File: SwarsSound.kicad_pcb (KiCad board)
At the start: 2 copper layers, 292.1 x 227.3 mm, 168 parts, among them P1 Main_Connector, P2 aud_con, P3 edge_con, Q1 2N3906f, Q2 2N3906f, Q3 2N3904, Q4 2N3904

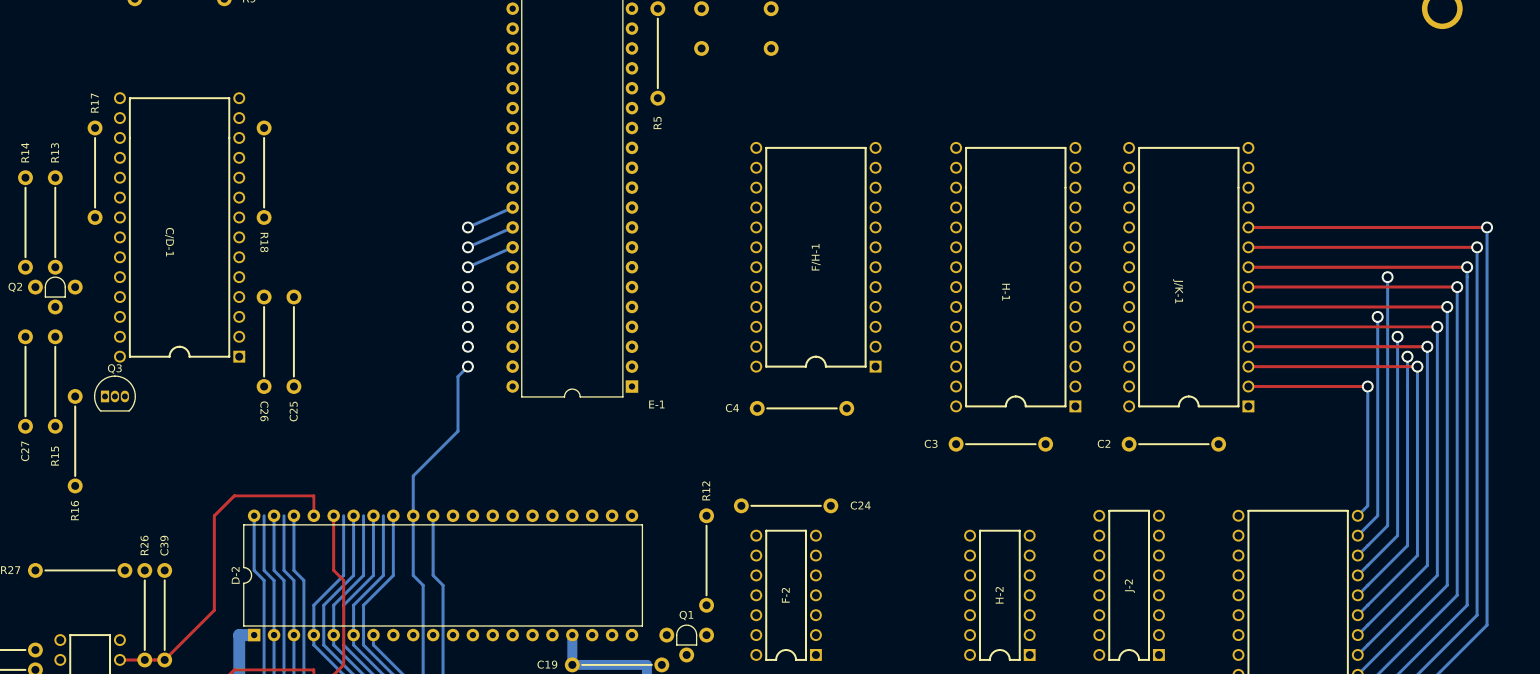
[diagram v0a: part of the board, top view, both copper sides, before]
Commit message: ROM and RAM buses
Not complete
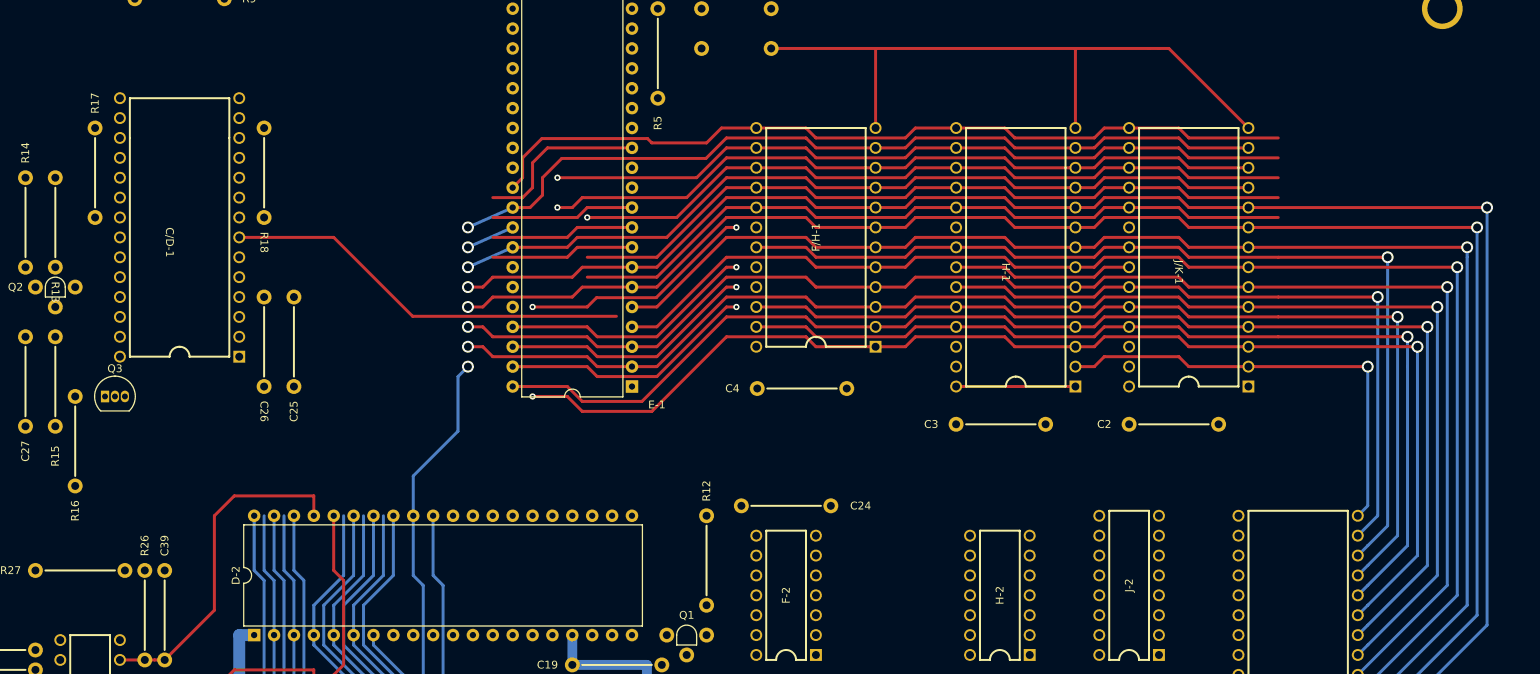
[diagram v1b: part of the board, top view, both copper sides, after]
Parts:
- moved C4 2.54 mm to (211.6, 87.9)
- moved F/H-1 2.54 mm to (212.7, 68.6)
- moved C2 2.54 mm to (259.1, 92.5)
- moved C3 2.54 mm to (237.0, 92.5)
- moved H-1 2.54 mm to (237.6, 71.1)
- moved J/K-1 2.54 mm to (259.7, 71.1)
- moved R13 1.27 mm to (115.6, 66.0), turned to 180 degrees
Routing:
- net SA4: track 77.1 -> 186.7 mm, vias 1 -> 2
- net SA5: track 152.1 -> 261.7 mm, vias 1 -> 2
- net SA1: track 179.6 -> 289.2 mm, vias 1 -> 2
- net SA0: track 180.2 -> 289.8 mm, vias 1 -> 2
- net GND: track 80.0 -> 188.7 mm
- net SD3: track 91.3 -> 196.8 mm
- net SA6: track 63.4 -> 167.8 mm
- net SD2: track 81.8 -> 183.4 mm
- net SA7: track 56.5 -> 157.8 mm, vias 1 -> 2
- net SD0: track 81.8 -> 182.1 mm
- net SD4: track 91.3 -> 187.6 mm, vias 0 -> 1
- net SD7: track 98.7 -> 193.3 mm
- net SD6: track 98.7 -> 193.3 mm
- net SD5: track 98.7 -> 192.2 mm, vias 0 -> 1
- net SD1: track 81.8 -> 175.3 mm, vias 1 -> 2
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
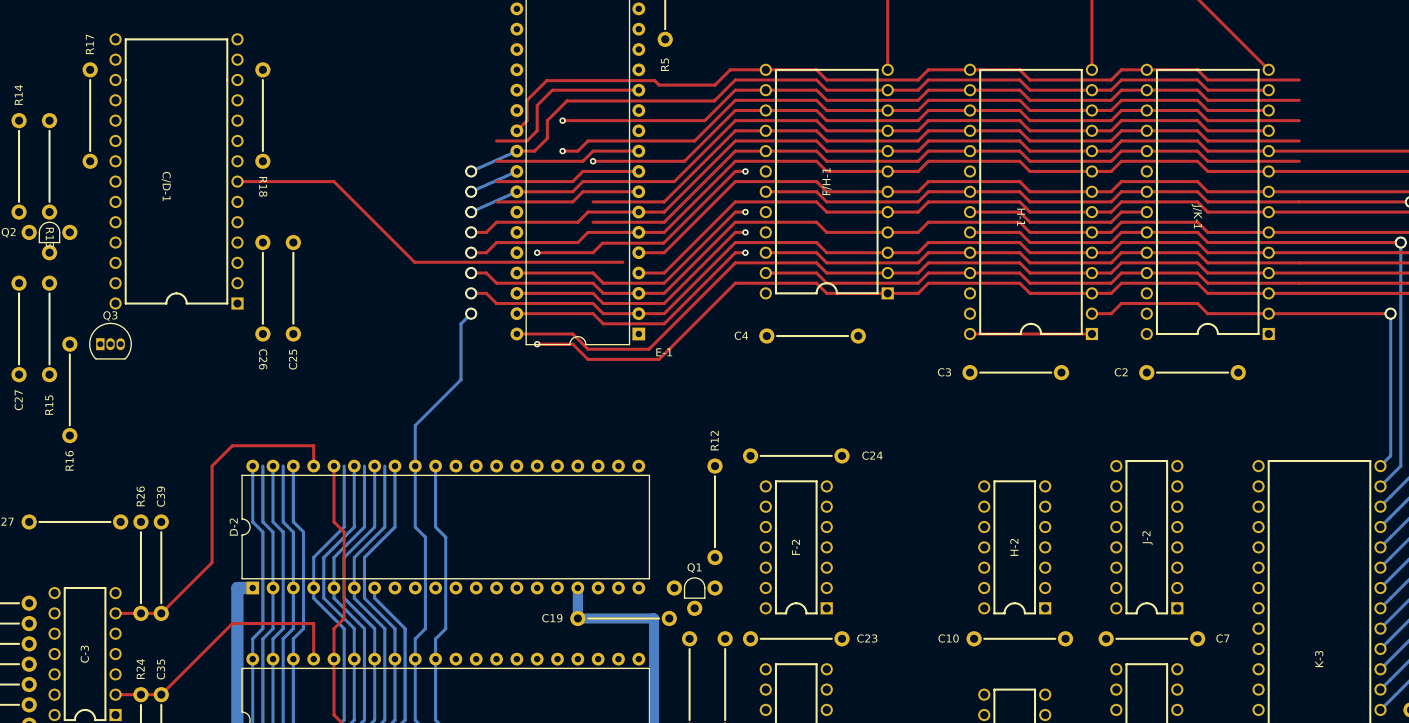
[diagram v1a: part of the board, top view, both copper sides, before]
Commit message: fixes
fixed RAM (pin '28' -> 24) and finished RAM/ROM data bus.
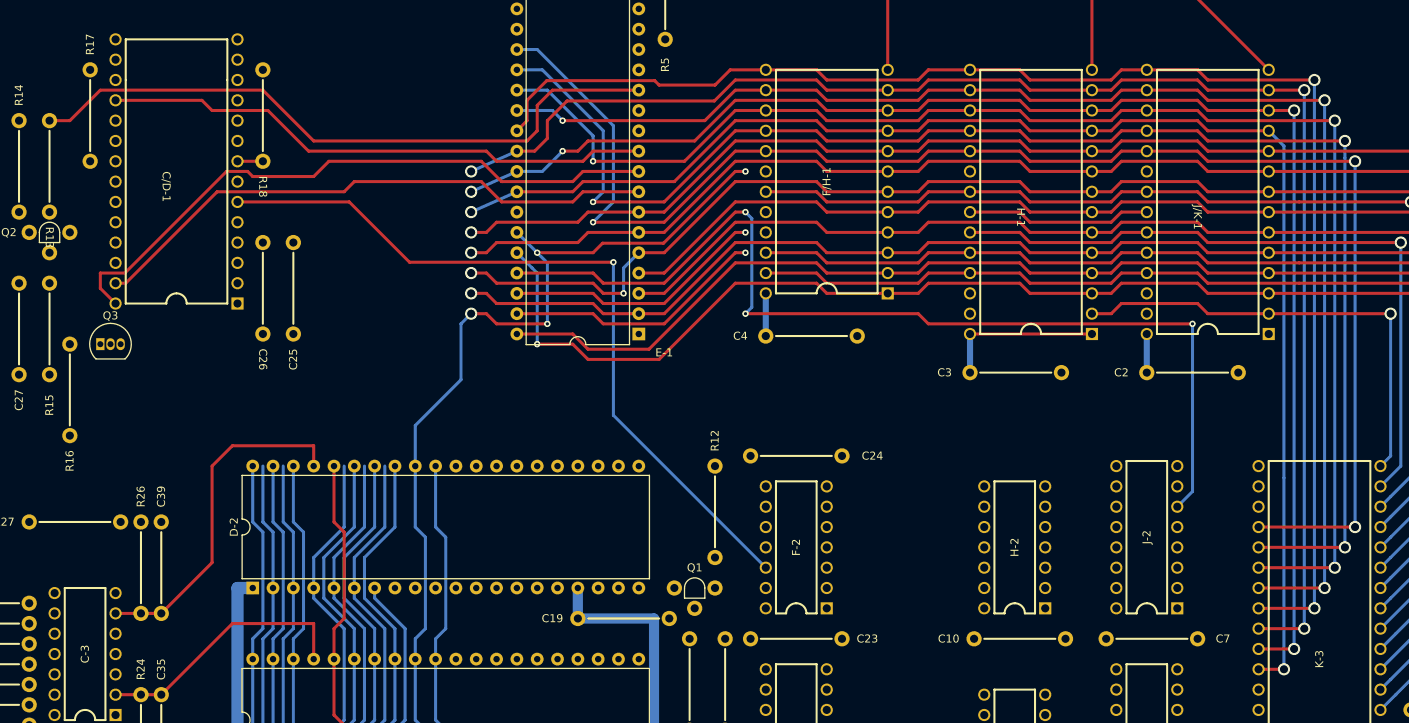
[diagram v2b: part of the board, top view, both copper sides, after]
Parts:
- moved C4 0.13 mm to (211.5, 87.9)
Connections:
- F/H-1 pad 24: (no net) -> +5V
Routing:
- net Net-(C/D-1-Pad6): track 0.00 -> 96.2 mm, vias 0 -> 1
- net SD7: track 193.3 -> 287.2 mm, vias 0 -> 3
- net ~PIA: track 32.8 -> 126.2 mm, vias 1 -> 3
- net SD6: track 193.3 -> 283.9 mm, vias 0 -> 3
- net SD5: track 192.2 -> 277.1 mm, vias 1 -> 3
- net (no net): track 82.6 -> 0.00 mm, vias 2 -> 0
- net SD1: track 175.3 -> 257.0 mm, vias 2 -> 4
- net SD4: track 187.6 -> 266.2 mm, vias 1 -> 3
- net SD2: track 183.4 -> 260.9 mm, vias 1 -> 3
- net SD3: track 196.8 -> 271.8 mm, vias 0 -> 2
- net SD0: track 182.1 -> 253.4 mm, vias 1 -> 2
- net PA1: track 18.3 -> 79.8 mm
- net PA5: track 22.3 -> 82.4 mm
- net PA0: track 18.3 -> 72.2 mm
- net SR\~W: track 97.5 -> 150.8 mm, vias 1 -> 4
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
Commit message: more traces
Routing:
- net +12V: track 0.00 -> 120.8 mm, vias 0 -> 1
- net -5V: track 87.4 -> 123.8 mm

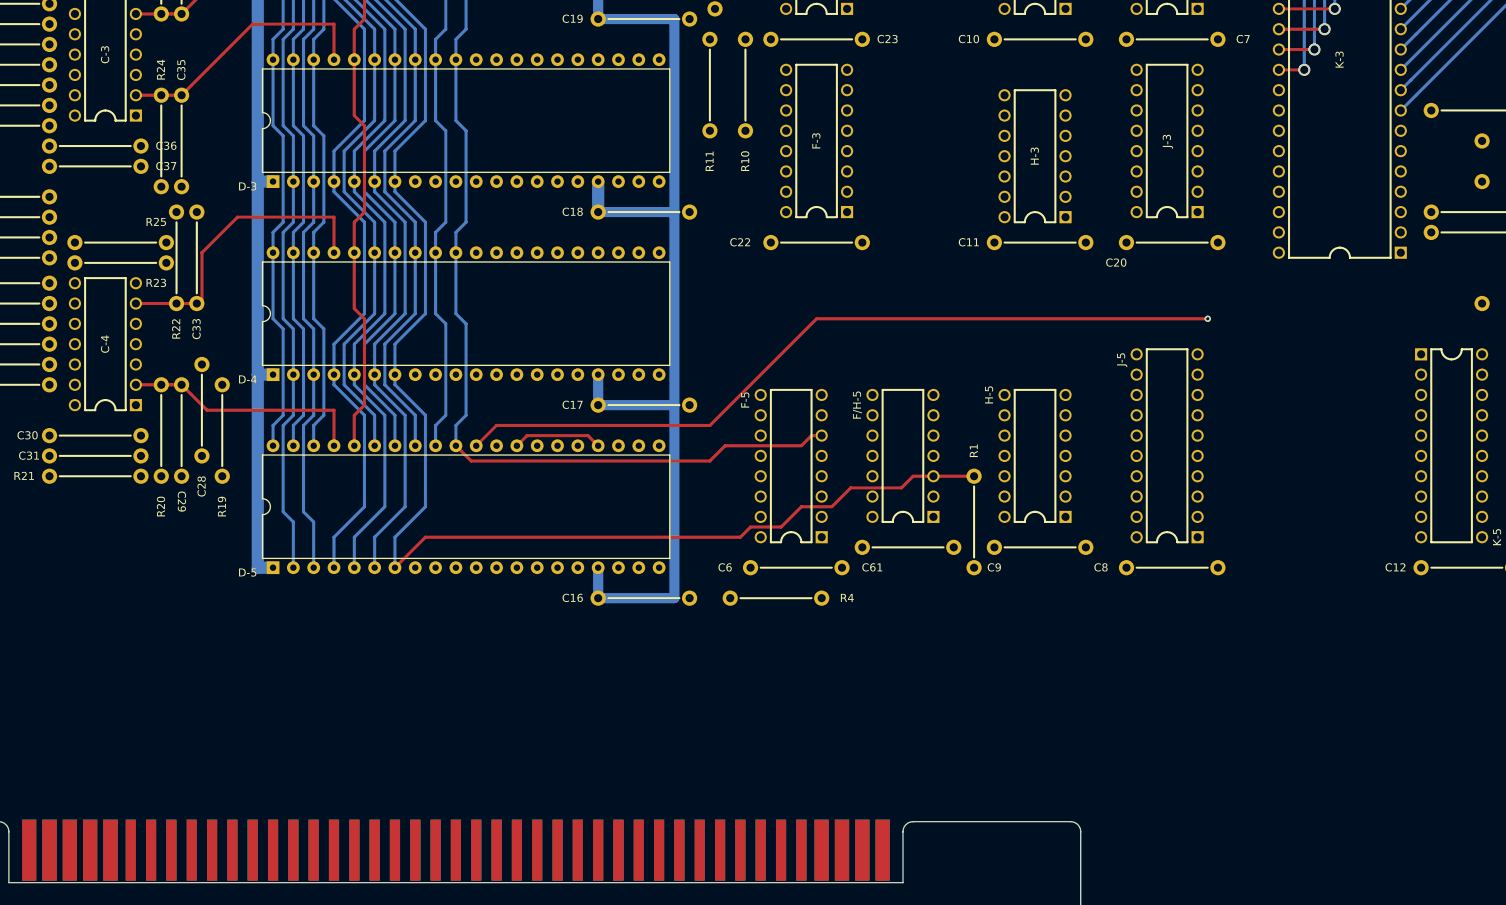
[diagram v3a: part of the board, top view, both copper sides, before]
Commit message: More traces on top done
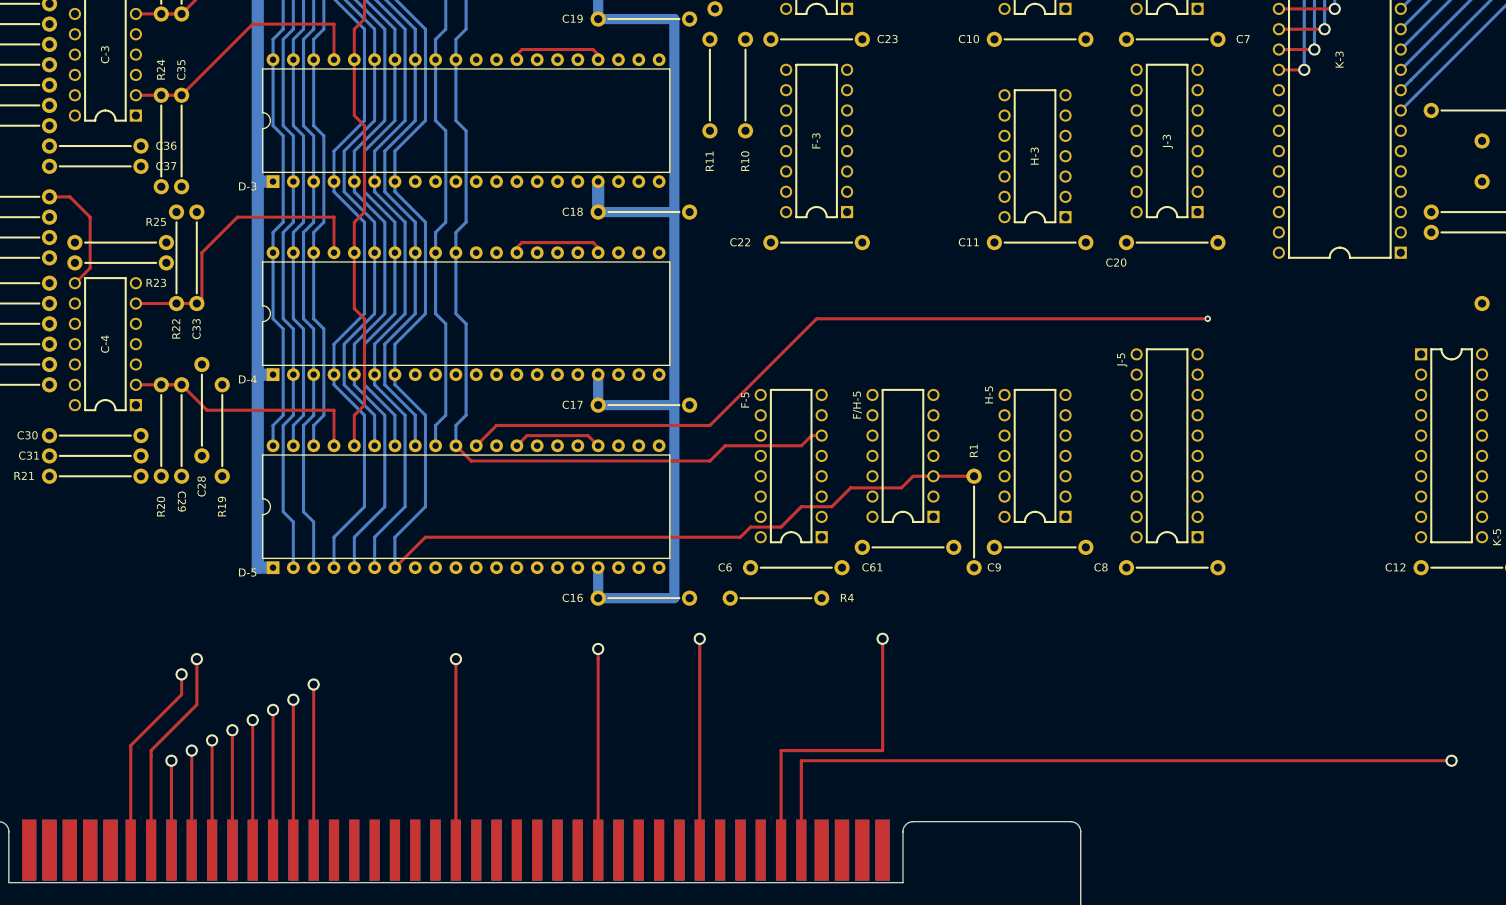
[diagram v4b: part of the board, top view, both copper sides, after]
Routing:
- net CLKQ: track 0.00 -> 92.5 mm, vias 0 -> 1
- net 1.5MHZ: track 0.00 -> 39.1 mm, vias 0 -> 1
- net 6MHZ: track 0.00 -> 26.4 mm, vias 0 -> 1
- net ~SOUNDRST: track 0.00 -> 26.2 mm, vias 0 -> 1
- net ~SOUND: track 0.00 -> 25.6 mm, vias 0 -> 1
- net R/~WB: track 0.00 -> 25.1 mm, vias 0 -> 1
- net AB0: track 0.00 -> 23.9 mm, vias 0 -> 1
- net PD0: track 0.00 -> 20.7 mm, vias 0 -> 1
- net PD1: track 0.00 -> 18.8 mm, vias 0 -> 1
- net PD2: track 0.00 -> 17.5 mm, vias 0 -> 1
- net PD3: track 0.00 -> 16.3 mm, vias 0 -> 1
- net PD4: track 0.00 -> 15.6 mm, vias 0 -> 1
- net SUM: track 0.00 -> 15.2 mm
- net PD5: track 0.00 -> 13.7 mm, vias 0 -> 1
- net PD6: track 0.00 -> 12.4 mm, vias 0 -> 1
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
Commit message: More traces completed
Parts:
- moved C56 1.27 mm to (95.2, 118.1), turned to 90 degrees
- moved C57 1.27 mm to (95.2, 115.6), turned to 90 degrees
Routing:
- net Net-(C56-Pad1): track 0.00 -> 8.78 mm
- net Net-(C48-Pad1): track 0.00 -> 5.72 mm
- net Net-(C-3-Pad8): track 0.00 -> 5.72 mm
- net Net-(C-3-Pad12): track 0.00 -> 5.71 mm
- net Net-(C-3-Pad10): track 0.00 -> 5.71 mm
- net AUD: track 0.00 -> 5.71 mm

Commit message: more traces on bottom completed
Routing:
- net P: track 156.2 -> 248.4 mm
- net +5V: track 156.0 -> 200.1 mm
- net Net-(F-2-Pad1): track 0.00 -> 3.81 mm
- net Net-(F-5-Pad10): track 0.00 -> 2.54 mm

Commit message: more traces
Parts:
- moved C47 1.91 mm to (29.2, 111.1), turned to 270 degrees
- moved R38 1.91 mm to (34.3, 120.0)
- moved R34 1.42 mm to (33.0, 131.4), turned to 90 degrees
- moved R44 1.42 mm to (85.1, 153.0), turned to 90 degrees
- moved R33 1.42 mm to (33.0, 134.0), turned to 90 degrees
- moved C46 0.63 mm to (31.8, 128.9)
- turned C53 to 180 degrees
- turned C54 to 180 degrees
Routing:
- net +12V: track 120.8 -> 211.8 mm
- net Net-(A-3-Pad12): track 0.00 -> 19.4 mm
- net Net-(A-3-Pad13): track 0.00 -> 17.6 mm
- net Net-(B-3-Pad8): track 0.00 -> 17.2 mm
- net Net-(A-3-Pad11): track 0.00 -> 15.5 mm

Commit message: more traces
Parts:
- moved R42 1.27 mm to (64.8, 147.3), turned to 90 degrees
- moved R43 1.27 mm to (64.8, 142.2), turned to 90 degrees
- turned C51 to 180 degrees
- turned C52 to 180 degrees
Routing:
- net AUD: track 5.71 -> 56.4 mm
- net Net-(B-3-Pad5): track 0.00 -> 27.9 mm
- net GND: track 188.7 -> 197.6 mm
- net Net-(R41-Pad1): track 0.00 -> 5.08 mm
